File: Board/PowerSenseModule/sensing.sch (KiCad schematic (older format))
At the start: 23 parts

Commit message: Using project library
Changed library ref to project not global
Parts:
- U?: symbol Power_Sense_Microchip_CUSTOM:MCP39F511A -> F1_Power_Sense:MCP39F511A
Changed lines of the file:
@@
 EESchema Schematic File Version 4
+LIBS:PowerSenseModule-cache
 EELAYER 29 0
 EELAYER END
@@
 $EndDescr
 $Comp
-L Power_Sense_Microchip_CUSTOM:MCP39F511A U?
+L F1_Power_Sense:MCP39F511A U?
 U 1 1 5D2177A0
 P 6700 3250
@@
 $EndComp
 $Comp
-L power:GNDD #PWR?
+L power:GNDD #PWR0116
 U 1 1 5D21F609
 P 8050 2100
-F 0 "#PWR?" H 8050 1850 50  0001 C CNN
+F 0 "#PWR0116" H 8050 1850 50  0001 C CNN
 F 1 "GNDD" H 8054 1945 50  0000 C CNN
 F 2 "" H 8050 2100 50  0001 C CNN
@@
 $EndComp
 $Comp
-L power:GNDA #PWR?
+L power:GNDA #PWR0117
 U 1 1 5D21F7BD
 P 5100 2100
-F 0 "#PWR?" H 5100 1850 50  0001 C CNN
+F 0 "#PWR0117" H 5100 1850 50  0001 C CNN
 F 1 "GNDA" H 5105 1927 50  0000 C CNN
 F 2 "" H 5100 2100 50  0001 C CNN
@@
 $EndComp
 $Comp
-L power:GNDA #PWR?
+L power:GNDA #PWR0118
 U 1 1 5D2201CD
 P 5450 2100
-F 0 "#PWR?" H 5450 1850 50  0001 C CNN
+F 0 "#PWR0118" H 5450 1850 50  0001 C CNN
 F 1 "GNDA" H 5455 1927 50  0000 C CNN
 F 2 "" H 5450 2100 50  0001 C CNN
@@
 Connection ~ 6850 1800
 $Comp
-L power:+3V3 #PWR?
+L power:+3V3 #PWR0119
 U 1 1 5D2207AA
 P 6850 1550
-F 0 "#PWR?" H 6850 1400 50  0001 C CNN
+F 0 "#PWR0119" H 6850 1400 50  0001 C CNN
 F 1 "+3V3" H 6865 1723 50  0000 C CNN
 F 2 "" H 6850 1550 50  0001 C CNN
@@
 	6850 1550 6850 1800
 $Comp
-L power:GNDA #PWR?
+L power:GNDA #PWR0120
 U 1 1 5D2218B8
 P 6600 4150
-F 0 "#PWR?" H 6600 3900 50  0001 C CNN
+F 0 "#PWR0120" H 6600 3900 50  0001 C CNN
 F 1 "GNDA" H 6605 3977 50  0000 C CNN
 F 2 "" H 6600 4150 50  0001 C CNN
@@
 $EndComp
 $Comp
-L power:GNDD #PWR?
+L power:GNDD #PWR0121
 U 1 1 5D22204E
 P 6800 4150
-F 0 "#PWR?" H 6800 3900 50  0001 C CNN
+F 0 "#PWR0121" H 6800 3900 50  0001 C CNN
 F 1 "GNDD" H 6804 3995 50  0000 C CNN
 F 2 "" H 6800 4150 50  0001 C CNN
@@
 	7550 3800 7550 4050
 $Comp
-L power:GNDA #PWR?
+L power:GNDA #PWR0122
 U 1 1 5D223DE6
 P 7550 4350
-F 0 "#PWR?" H 7550 4100 50  0001 C CNN
+F 0 "#PWR0122" H 7550 4100 50  0001 C CNN
 F 1 "GNDA" H 7555 4177 50  0000 C CNN
 F 2 "" H 7550 4350 50  0001 C CNN
@@
 $EndComp
 $Comp
-L power:GNDA #PWR?
+L power:GNDA #PWR0123
 U 1 1 5D2243A8
 P 7900 4350
-F 0 "#PWR?" H 7900 4100 50  0001 C CNN
+F 0 "#PWR0123" H 7900 4100 50  0001 C CNN
 F 1 "GNDA" H 7905 4177 50  0000 C CNN
 F 2 "" H 7900 4350 50  0001 C CNN
@@
 $EndComp
 $Comp
-L power:+3V3 #PWR?
+L power:+3V3 #PWR0124
 U 1 1 5D22706A
 P 5200 4200
-F 0 "#PWR?" H 5200 4050 50  0001 C CNN
+F 0 "#PWR0124" H 5200 4050 50  0001 C CNN
 F 1 "+3V3" H 5215 4373 50  0000 C CNN
 F 2 "" H 5200 4200 50  0001 C CNN
@@
 $EndComp
 $Comp
-L power:GNDA #PWR?
+L power:GNDA #PWR0125
 U 1 1 5D2279C0
 P 5200 4800
-F 0 "#PWR?" H 5200 4550 50  0001 C CNN
+F 0 "#PWR0125" H 5200 4550 50  0001 C CNN
 F 1 "GNDA" H 5205 4627 50  0000 C CNN
 F 2 "" H 5200 4800 50  0001 C CNN
@@
 $EndComp
 $Comp
-L power:GNDA #PWR?
+L power:GNDA #PWR0126
 U 1 1 5D26D7C8
 P 3800 2900
-F 0 "#PWR?" H 3800 2650 50  0001 C CNN
+F 0 "#PWR0126" H 3800 2650 50  0001 C CNN
 F 1 "GNDA" H 3805 2727 50  0000 C CNN
 F 2 "" H 3800 2900 50  0001 C CNN
@@
 $EndComp
 $Comp
-L power:GNDA #PWR?
+L power:GNDA #PWR0127
 U 1 1 5D26DECF
 P 3300 2900
-F 0 "#PWR?" H 3300 2650 50  0001 C CNN
+F 0 "#PWR0127" H 3300 2650 50  0001 C CNN
 F 1 "GNDA" H 3305 2727 50  0000 C CNN
 F 2 "" H 3300 2900 50  0001 C CNN
@@
 	4050 3550 4050 3850
 $Comp
-L power:GNDA #PWR?
+L power:GNDA #PWR0128
 U 1 1 5D282E96
 P 4050 4150
-F 0 "#PWR?" H 4050 3900 50  0001 C CNN
+F 0 "#PWR0128" H 4050 3900 50  0001 C CNN
 F 1 "GNDA" H 4055 3977 50  0000 C CNN
 F 2 "" H 4050 4150 50  0001 C CNN
@@
 $EndComp
 $Comp
-L power:GNDA #PWR?
+L power:GNDA #PWR0129
 U 1 1 5D283600
 P 3250 4150
-F 0 "#PWR?" H 3250 3900 50  0001 C CNN
+F 0 "#PWR0129" H 3250 3900 50  0001 C CNN
 F 1 "GNDA" H 3255 3977 50  0000 C CNN
 F 2 "" H 3250 4150 50  0001 C CNN
@@
 	4450 3550 4600 3550
 $Comp
-L power:GNDA #PWR?
+L power:GNDA #PWR0130
 U 1 1 5D24546D
 P 3650 4150
-F 0 "#PWR?" H 3650 3900 50  0001 C CNN
+F 0 "#PWR0130" H 3650 3900 50  0001 C CNN
 F 1 "GNDA" H 3655 3977 50  0000 C CNN
 F 2 "" H 3650 4150 50  0001 C CNN
@@
 $EndComp
 $Comp
-L power:GNDA #PWR?
+L power:GNDA #PWR0131
 U 1 1 5D245980
 P 4450 4150
-F 0 "#PWR?" H 4450 3900 50  0001 C CNN
+F 0 "#PWR0131" H 4450 3900 50  0001 C CNN
 F 1 "GNDA" H 4455 3977 50  0000 C CNN
 F 2 "" H 4450 4150 50  0001 C CNN

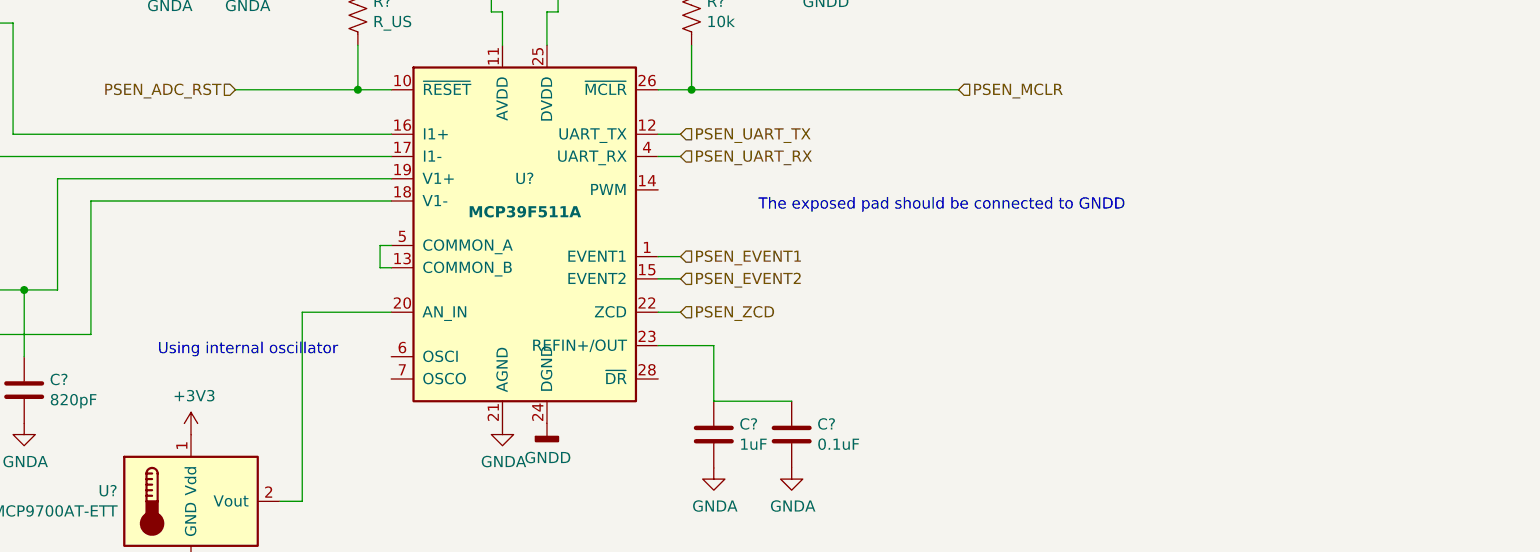
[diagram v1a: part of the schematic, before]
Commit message: Changed power connector and added CAN nets
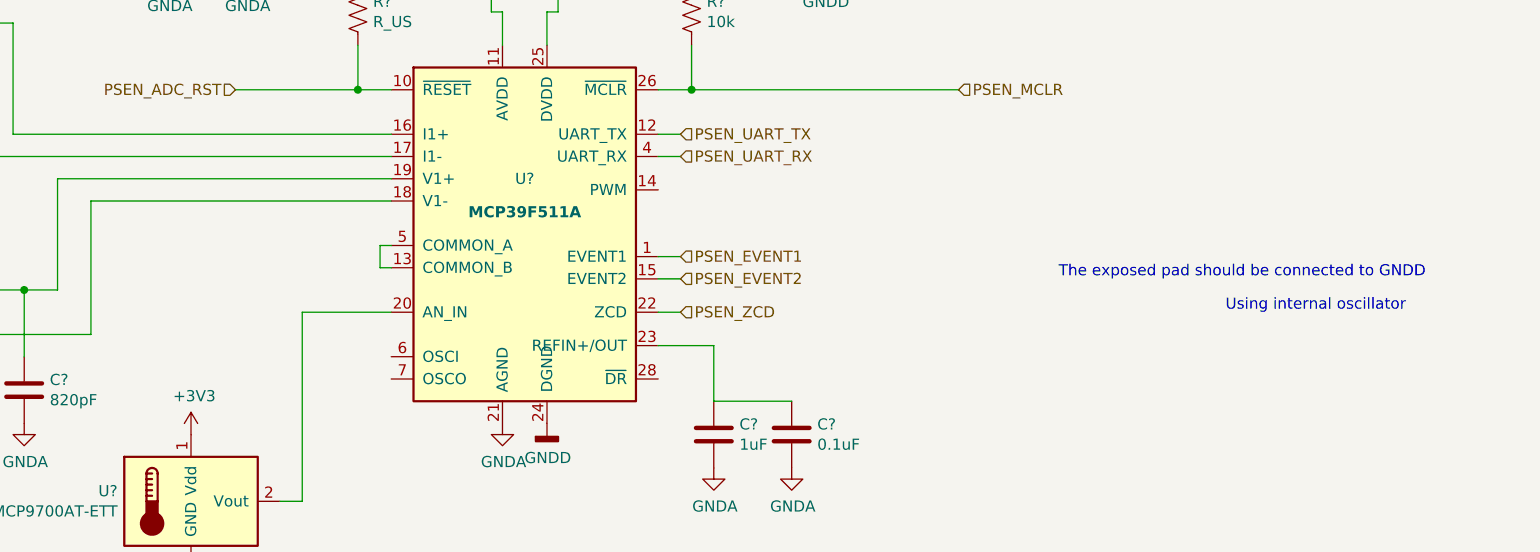
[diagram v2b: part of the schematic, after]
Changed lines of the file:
@@
 	1    0    0    -1
 $EndComp
-Text Notes 7750 3200 0    50   ~ 0
+Text Notes 9100 3500 0    50   ~ 0
 The exposed pad should be connected to GNDD\n
-Text Notes 5050 3850 0    50   ~ 0
+Text Notes 9850 3650 0    50   ~ 0
 Using internal oscillator\n
 $Comp

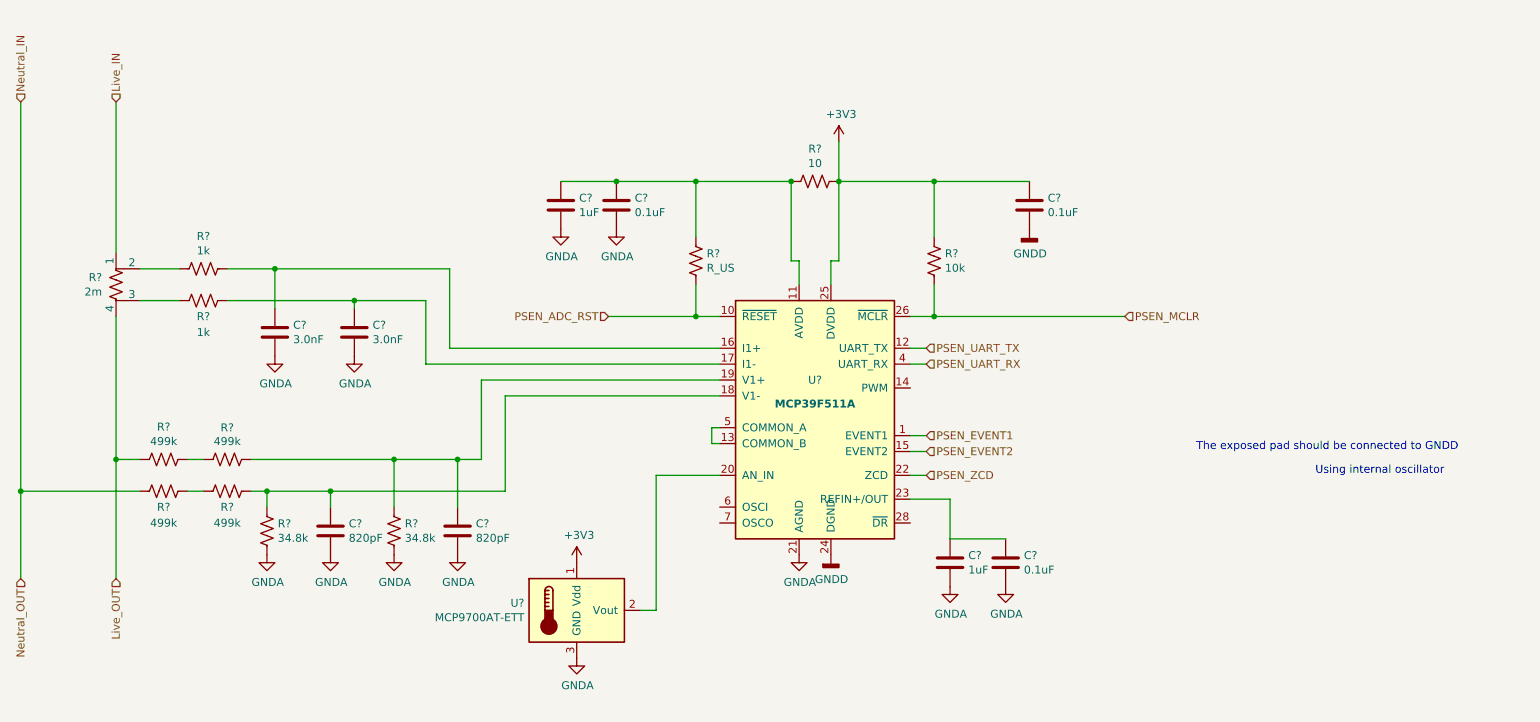
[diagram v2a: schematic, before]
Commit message: Added linear reg, cleaned up schematic
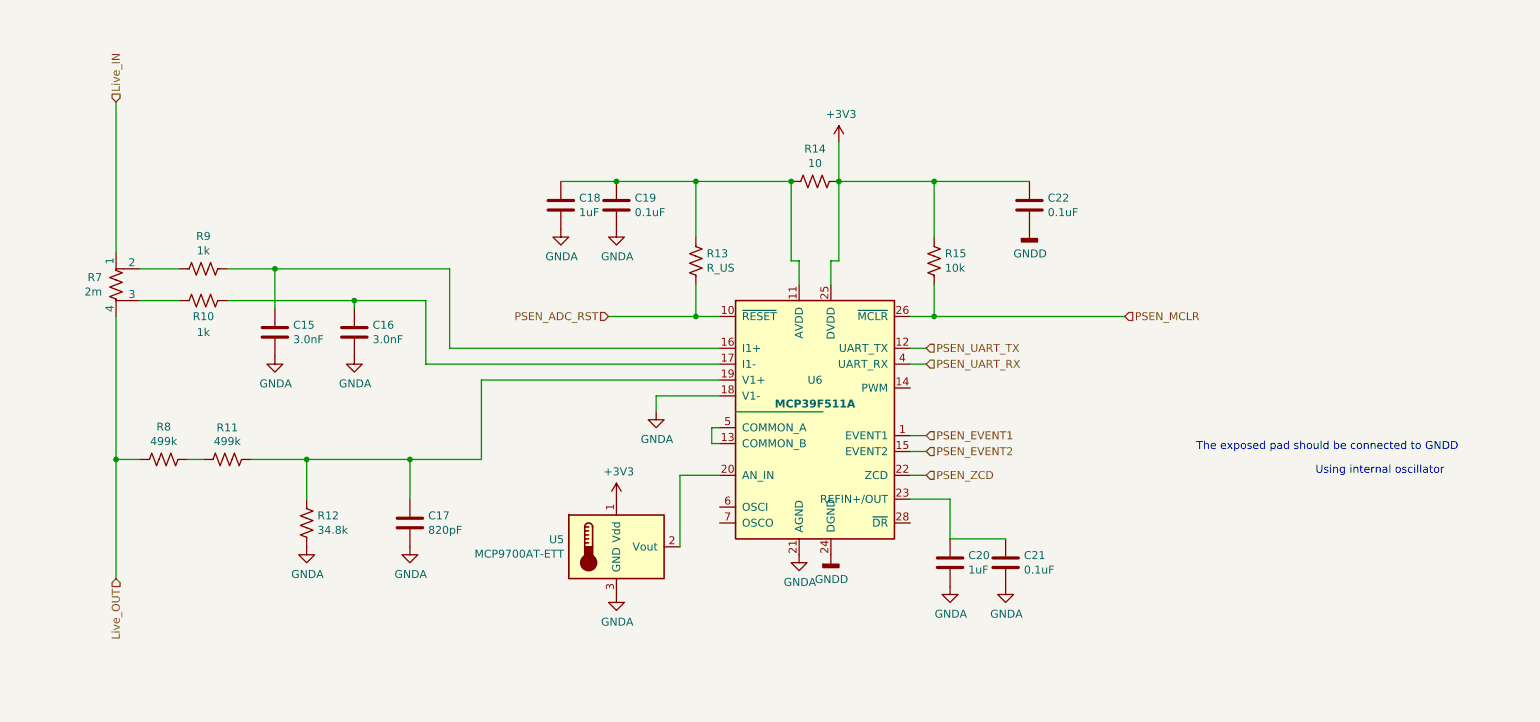
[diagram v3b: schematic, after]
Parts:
- removed C?: 820pF, symbol Device:C
- removed R? (x2): 499k, symbol Device:R_US
- removed R?: 34.8k, symbol Device:R_US
- gave numbers to parts that had none: 19
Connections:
- net GNDA: now also U6.18 (V1-)
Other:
- moved on the sheet: C17, R12, U5

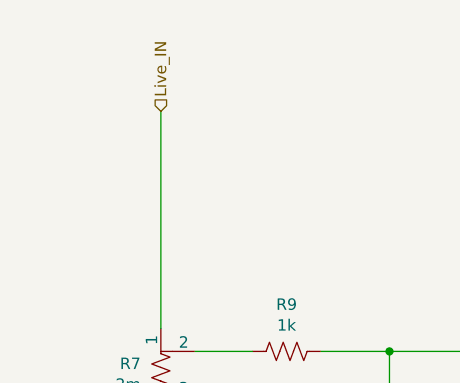
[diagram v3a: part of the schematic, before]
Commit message: Lin Reg Connected with cap, global power net, and wiring.
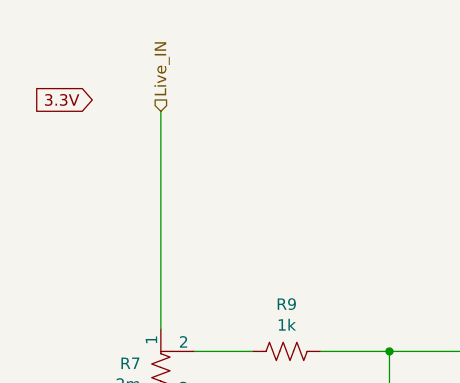
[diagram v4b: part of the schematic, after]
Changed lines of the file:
@@
 Wire Wire Line
 	5850 3650 6100 3650
+Text GLabel 2000 1250 0    50   Input ~ 0
+3.3V
 $EndSCHEMATC

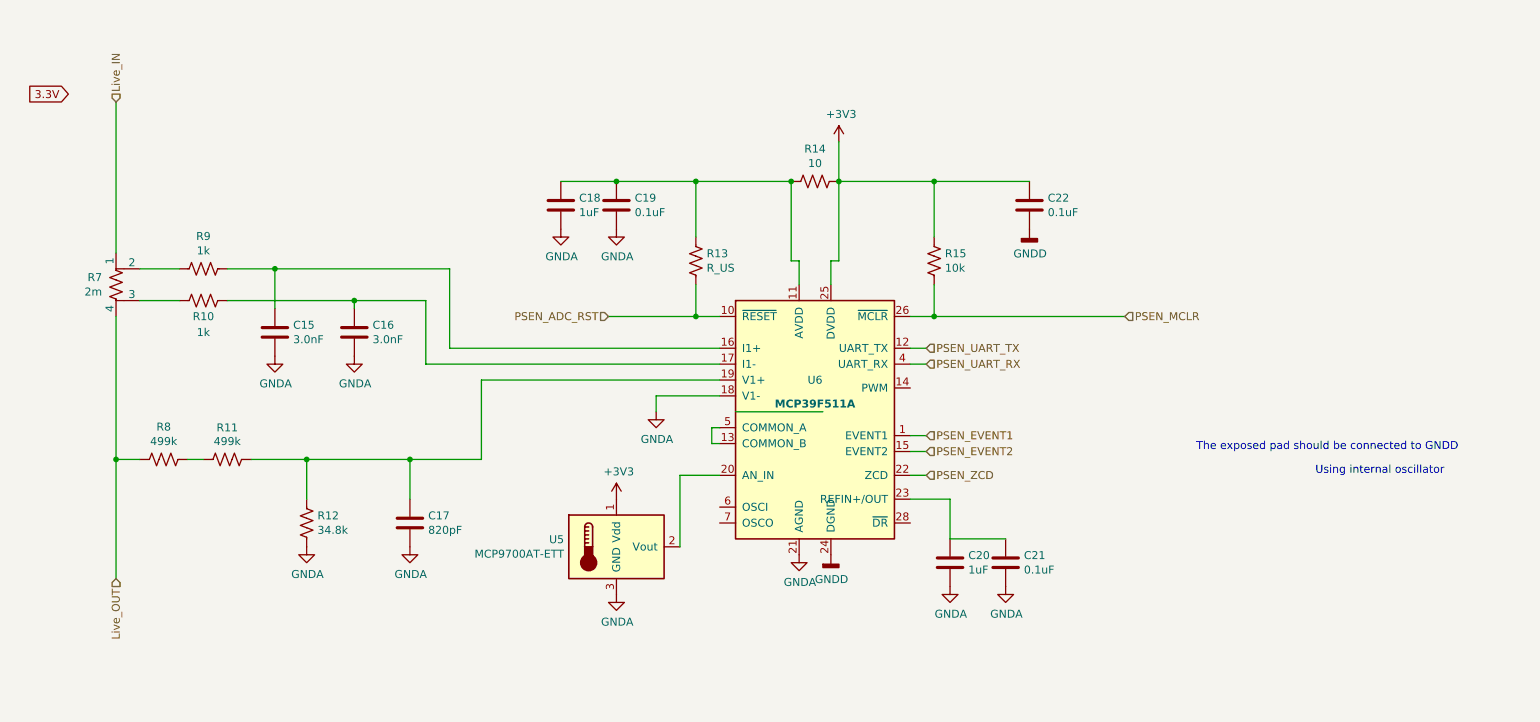
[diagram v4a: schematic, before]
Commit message: Finalizing footprints - a
Changed footprints of 4.7u, 10u, 47u ceramic caps to 0805 from 0603.

Changed output cap of linear reg to 150u electrolytic 

Added tie net for grounds

Connector footprints

Added notes

TODO:
footprints of net tie, 150u electrolytic
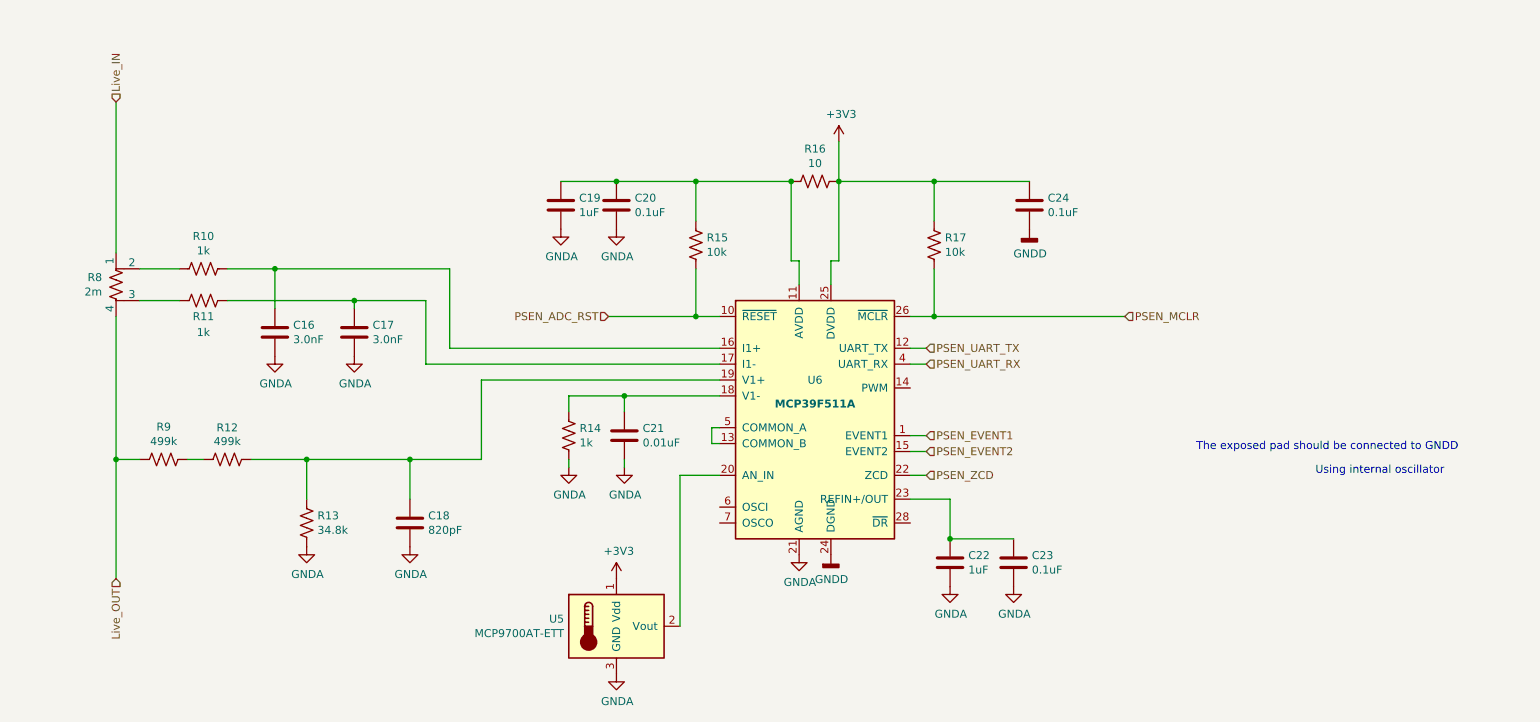
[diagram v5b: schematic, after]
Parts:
- added C21: 0.01uF, Capacitor_SMD:C_0603_1608Metric_Pad1.05x0.95mm_HandSolder, symbol Device:C
- added R14: 1k, symbol Device:R_US
- C16: renamed from C15; footprint (none) -> Capacitor_SMD:C_0603_1608Metric_Pad1.05x0.95mm_HandSolder
- C17: renamed from C16; footprint (none) -> Capacitor_SMD:C_0603_1608Metric_Pad1.05x0.95mm_HandSolder
- C18: renamed from C17; footprint (none) -> Capacitor_SMD:C_0603_1608Metric_Pad1.05x0.95mm_HandSolder
- C19: renamed from C18; footprint (none) -> Capacitor_SMD:C_0603_1608Metric_Pad1.05x0.95mm_HandSolder
- C20: renamed from C19; footprint (none) -> Capacitor_SMD:C_0603_1608Metric_Pad1.05x0.95mm_HandSolder
- C22: renamed from C20; footprint (none) -> Capacitor_SMD:C_0603_1608Metric_Pad1.05x0.95mm_HandSolder
- C23: renamed from C21; footprint (none) -> Capacitor_SMD:C_0603_1608Metric_Pad1.05x0.95mm_HandSolder
- C24: renamed from C22; footprint (none) -> Capacitor_SMD:C_0603_1608Metric_Pad1.05x0.95mm_HandSolder
- R10: renamed from R9; footprint (none) -> Resistor_SMD:R_0603_1608Metric_Pad1.05x0.95mm_HandSolder
- R11: renamed from R10; footprint (none) -> Resistor_SMD:R_0603_1608Metric_Pad1.05x0.95mm_HandSolder
- R12: renamed from R11; footprint (none) -> Resistor_SMD:R_0603_1608Metric_Pad1.05x0.95mm_HandSolder
- R13: renamed from R12; footprint (none) -> Resistor_SMD:R_0603_1608Metric_Pad1.05x0.95mm_HandSolder
- R15: renamed from R13; value R_US -> 10k; footprint (none) -> Resistor_SMD:R_0603_1608Metric_Pad1.05x0.95mm_HandSolder
- R16: renamed from R14; footprint (none) -> Resistor_SMD:R_0603_1608Metric_Pad1.05x0.95mm_HandSolder
- R17: renamed from R15; footprint (none) -> Resistor_SMD:R_0603_1608Metric_Pad1.05x0.95mm_HandSolder
- R8: renamed from R7; footprint (none) -> Resistor_SMD:R_0603_1608Metric_Pad1.05x0.95mm_HandSolder
- R9: renamed from R8; footprint (none) -> Resistor_SMD:R_0603_1608Metric_Pad1.05x0.95mm_HandSolder
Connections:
- net GNDA: now also C21.2, R14.2; no longer U6.18 (V1-)
- new net: C21.1, R14.1, U6.18 (V1-)
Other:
- moved on the sheet: C23, R15, R17, U5

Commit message: Finalizing Footprints PT B
Have two copies of everything, don't know why. Added NETI to remaining resistors and capacitor. Let's see
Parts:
- R14: footprint (none) -> Resistor_SMD:R_0603_1608Metric_Pad1.05x0.95mm_HandSolder
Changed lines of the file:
@@
 F 0 "R14" H 5218 3446 50  0000 L CNN
 F 1 "1k" H 5218 3355 50  0000 L CNN
-F 2 "" V 5190 3390 50  0001 C CNN
+F 2 "Resistor_SMD:R_0603_1608Metric_Pad1.05x0.95mm_HandSolder" V 5190 3390 50  0001 C CNN
 F 3 "~" H 5150 3400 50  0001 C CNN
 	1    5150 3400

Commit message: Changed R8 to be a 4 pin shunt resistor
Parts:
- R8: footprint Resistor_SMD:R_0603_1608Metric_Pad1.05x0.95mm_HandSolder -> Resistor_SMD:R_Shunt_Vishay_WSK2512_6332Metric_T1.19mm
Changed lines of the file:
@@
 F 0 "R8" H 2212 2496 50  0000 R CNN
 F 1 "2m" H 2212 2405 50  0000 R CNN
-F 2 "Resistor_SMD:R_0603_1608Metric_Pad1.05x0.95mm_HandSolder" V 2230 2450 50  0001 C CNN
+F 2 "Resistor_SMD:R_Shunt_Vishay_WSK2512_6332Metric_T1.19mm" V 2230 2450 50  0001 C CNN
 F 3 "~" H 2300 2450 50  0001 C CNN
 	1    2300 2450
